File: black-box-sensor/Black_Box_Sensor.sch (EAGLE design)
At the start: 58 parts, among them J1 104031-0811, J2 UX60-MB-5S8, J3 B4B-PH-SM4-TBT(LF)(SN), U1 ADXL375, U2 ADXL375, U3 ATMEGA32U4-AU, U4 FXAS21002CQR1, U6 NL27WZ32USG, U7 LT1129CST-5#PBF, U8 AD8426ACPZ-WP, U9 TXU0304

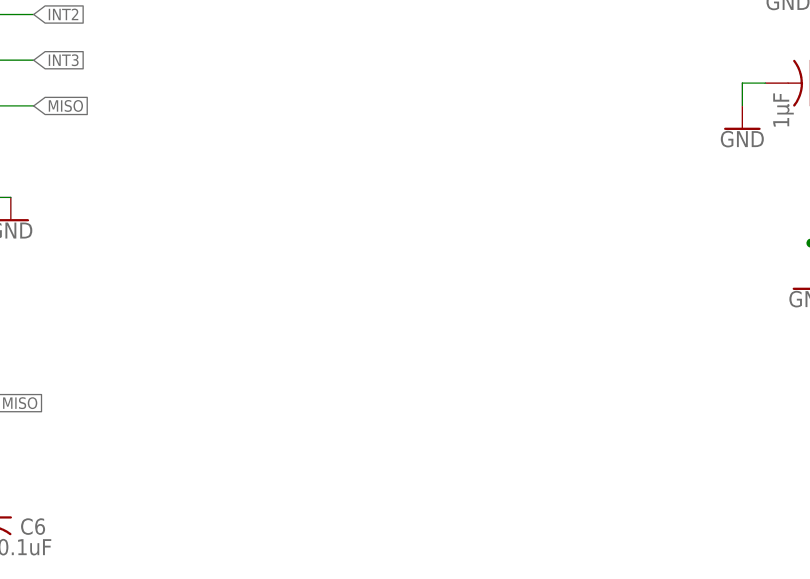
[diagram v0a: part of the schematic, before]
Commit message: Gyroscope added to schematic
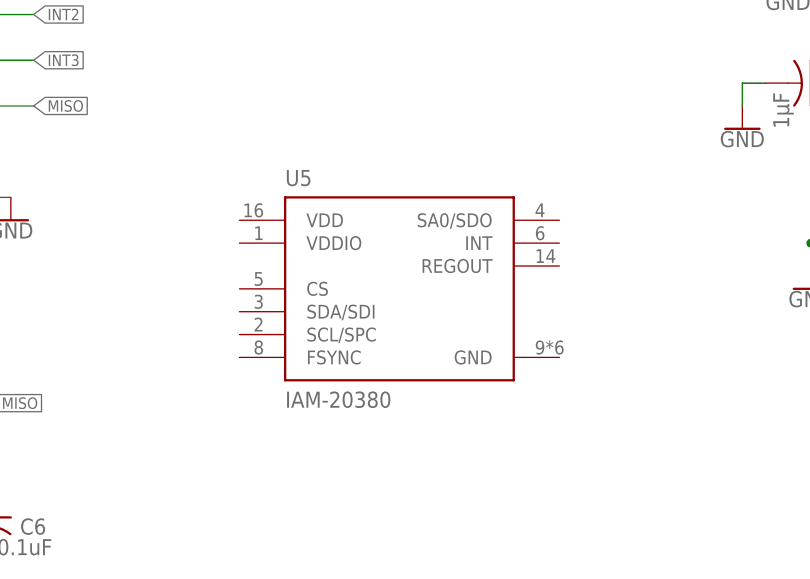
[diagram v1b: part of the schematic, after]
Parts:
- added U5: IAM-20380, BBS_Library:IAM-20380
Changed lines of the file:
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@@
 <part name="P+9" library="supply1" library_urn="urn:adsk.eagle:library:371" deviceset="+5V" device=""/>
 <part name="R16" library="rcl" library_urn="urn:adsk.eagle:library:334" deviceset="R-US_" device="R0603" package3d_urn="urn:adsk.eagle:package:23555/3" value="10k"/>
+<part name="U5" library="BBS_Library" deviceset="IAM-20380" device=""/>
 </parts>
 <sheets>
@@
 <attribute name="VALUE" x="170.942" y="92.71" size="1.778" layer="96" rot="R90"/>
 </instance>
+<instance part="U5" gate="G$1" x="114.3" y="25.4" smashed="yes">
+<attribute name="NAME" x="101.6" y="36.83" size="1.778" layer="95"/>
+<attribute name="VALUE" x="101.6" y="13.97" size="1.78078125" layer="96" align="top-left"/>
+</instance>
 </instances>

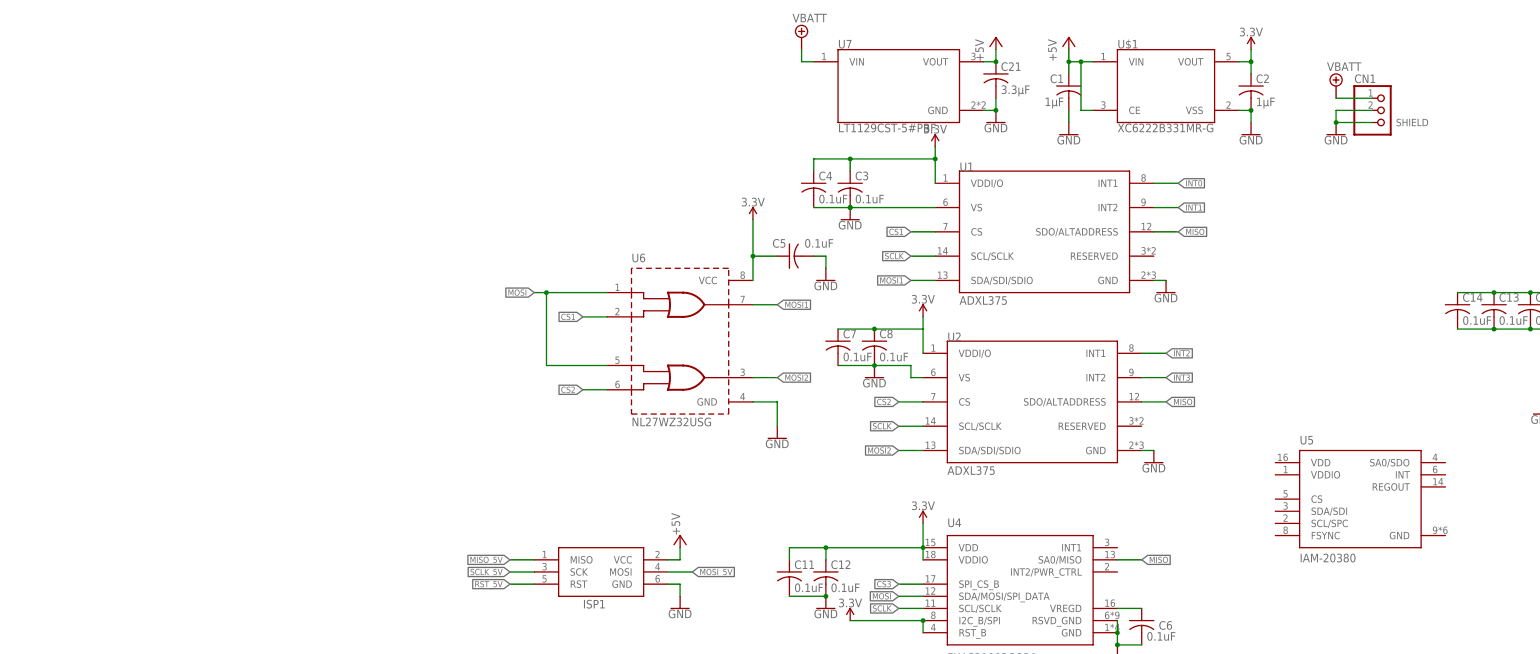
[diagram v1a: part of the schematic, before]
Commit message: Added gyroscope
missing some connections, and its capacitors may not have the right footprint, will follow up with Valentin later about it
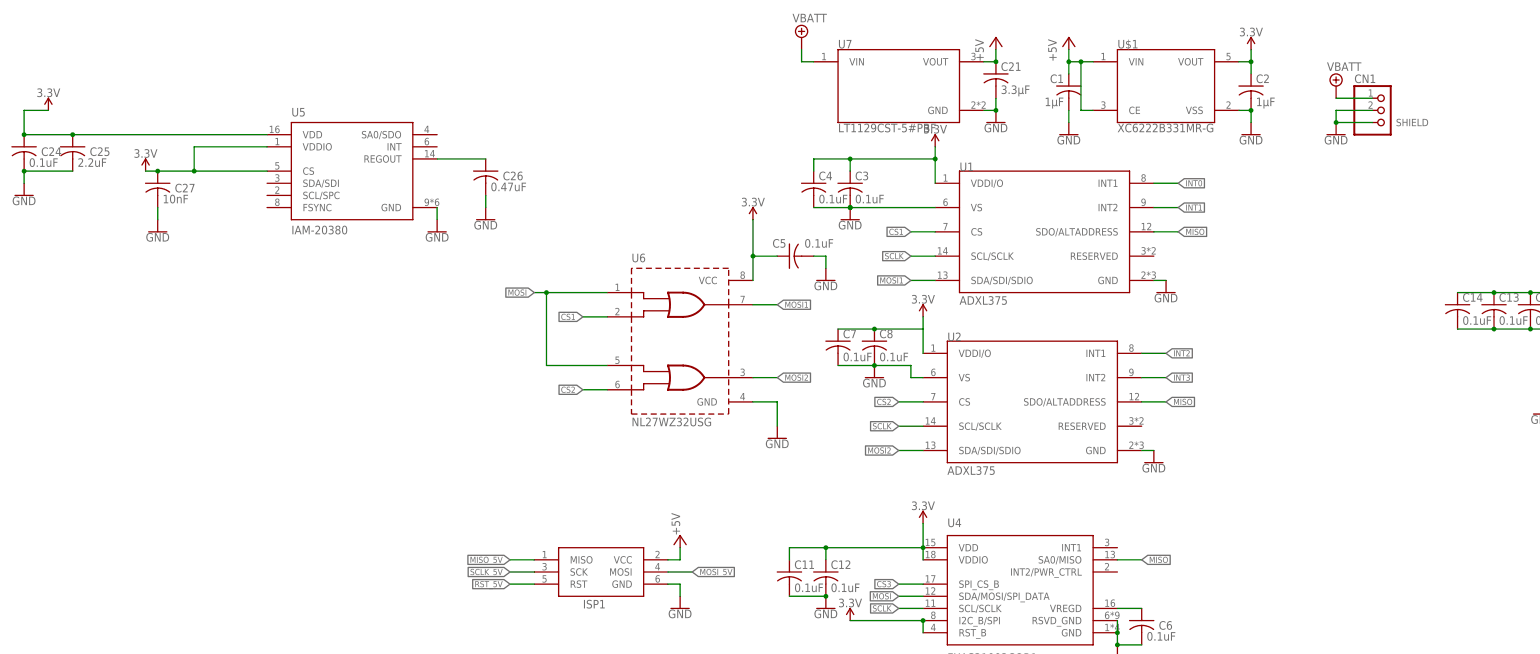
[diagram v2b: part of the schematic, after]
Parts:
- added C24: 0.1uF, rcl:C-USC0603
- added C25: 2.2uF, rcl:C-USC0603
- added C26: 0.47uF, rcl:C-USC0603
- added C27: 10nF, rcl:C-USC0603
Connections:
- new net N$10: C26.1, U5.REGOUT
- net 3.3V: now also C24.1, C25.1, C27.1, U5.CS, U5.VDD, U5.VDDIO
- net GND: now also C24.2, C25.2, C26.2, C27.2, U5.GND
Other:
- moved on the sheet: U5

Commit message: Gyroscope wiring complete
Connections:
- new net FSYNC_GYRO: U3.PB4(ADC11)
- new net INT6: U3.PE6(INT.6/AIN0)
- new net N$11: U5.INT
- new net N$12: U5.FSYNC
- net GND: now also U5.SA0/SDO
- net INT0: now also U5.SCL/SPC
- net INT1: now also U5.SDA/SDI

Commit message: clean schematic for DR
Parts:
- removed C11, C12: 0.1uF, rcl:C-USC0603K
- removed C6: 0.1uF, rcl:C-USC0603
- removed U4: FXAS21002CQR1, BBS_Library:FXAS21002CQR1
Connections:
- removed net FSYNC_GYRO: U3.PB4(ADC11)
- removed net N$1: C6.1, U4.VREGD
- removed net N$11: U5.INT
- removed net N$12: U5.FSYNC
- new net FSYNC: U3.PB4(ADC11), U5.FSYNC
- net 3.3V: no longer C11.1, C12.1, U4.I2C_B/SPI, U4.RST_B, U4.VDD, U4.VDDIO
- net CS3: no longer U4.SPI_CS_B
- net GND: no longer C11.2, C12.2, C6.2, U4.GND, U4.RSVD_GND
- net INT6: now also U5.INT
- net MISO: no longer U4.SA0/MISO
- net MOSI: no longer U4.SDA/MOSI/SPI_DATA
- net SCLK: no longer U4.SCL/SCLK
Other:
- moved on the sheet: C1, C18, C19, C2, C21, C24, C25, C26, C27, CN1, J3, JP1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

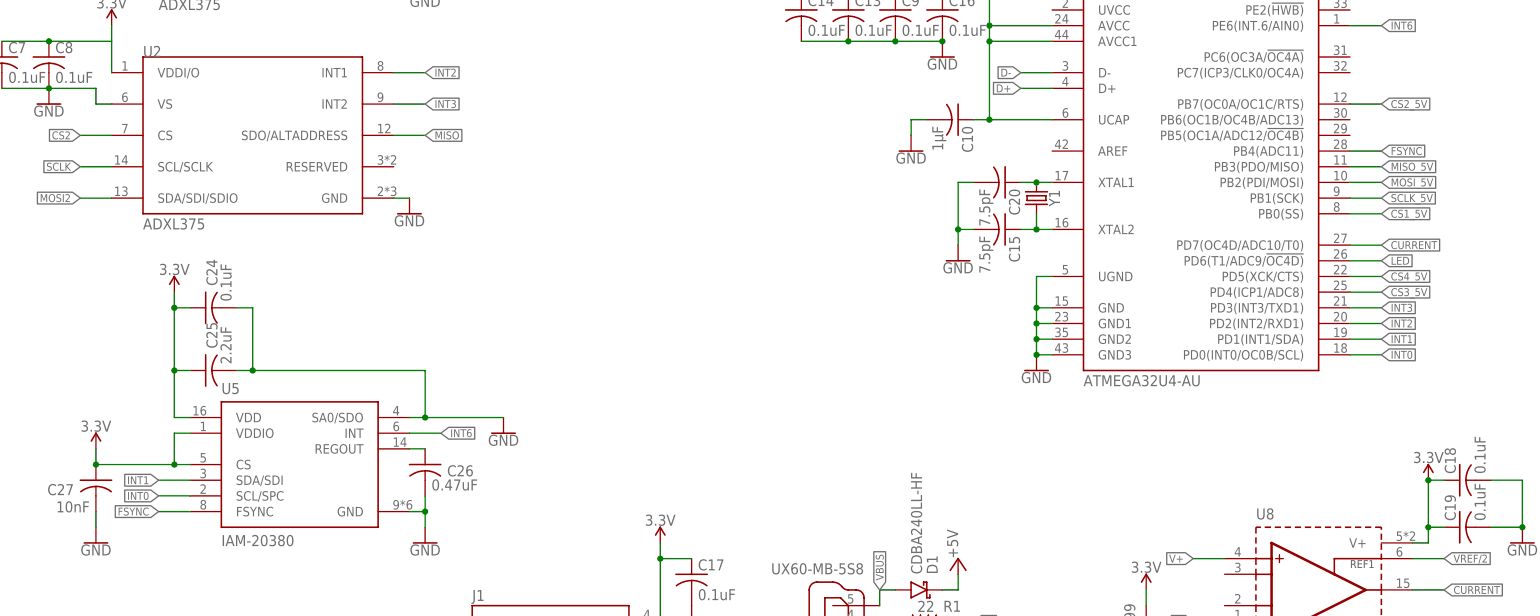
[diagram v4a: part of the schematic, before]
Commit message: fix some pin connections, but possibly will switch microcontroller
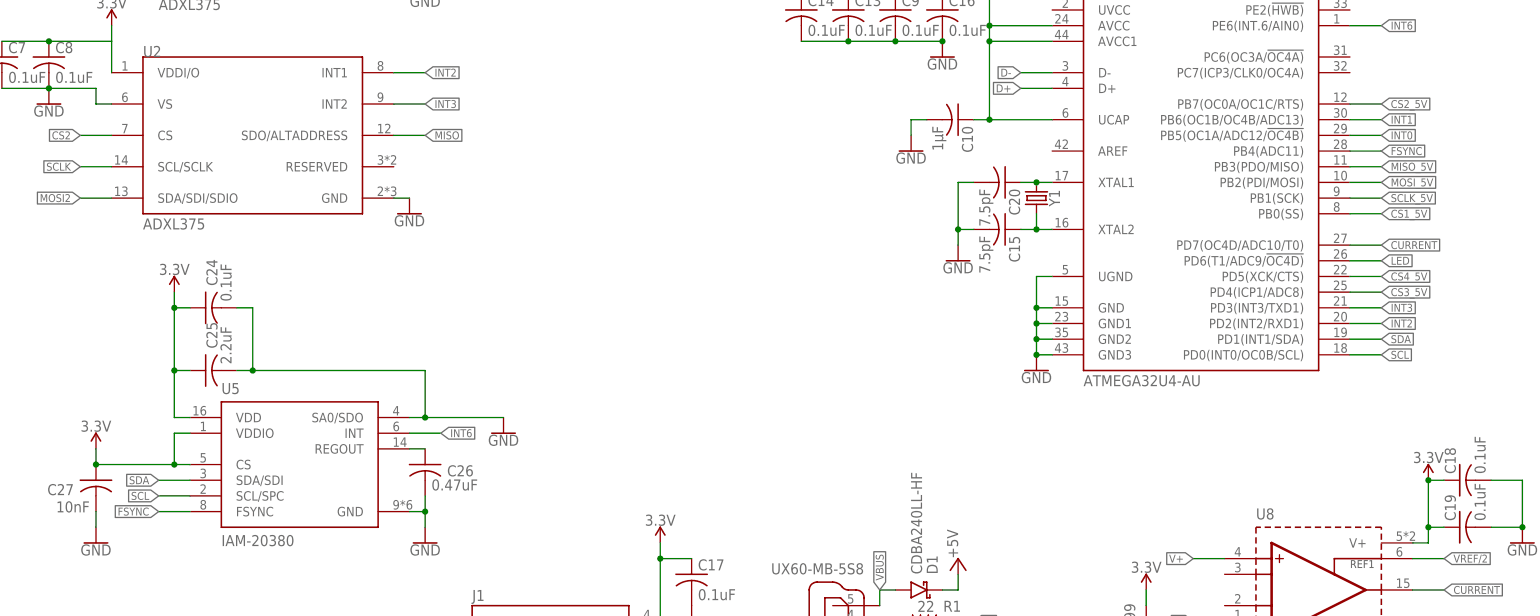
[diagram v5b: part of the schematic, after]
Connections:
- new net SCL: U3.PD0(INT0/OC0B/SCL), U5.SCL/SPC
- new net SDA: U3.PD1(INT1/SDA), U5.SDA/SDI
- net INT0: now also U3.PB5(OC1A/ADC12/!OC4B); no longer U3.PD0(INT0/OC0B/SCL), U5.SCL/SPC
- net INT1: now also U3.PB6(OC1B/OC4B/ADC13); no longer U3.PD1(INT1/SDA), U5.SDA/SDI
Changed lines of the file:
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@@
 </segment>
 </net>
-<net name="INT1" class="0">
+<net name="SDA" class="0">
 <segment>
 <pinref part="U3" gate="G$1" pin="PD1(INT1/SDA)"/>
@@
 </segment>
 <segment>
-<pinref part="U1" gate="ADXL375BCCZ-RL7" pin="INT2"/>
-<wire x1="71.12" y1="86.36" x2="76.2" y2="86.36" width="0.1524" layer="91"/>
-<label x="76.2" y="86.36" size="1.27" layer="95" xref="yes"/>
-</segment>
-<segment>
 <wire x1="35.56" y1="-10.16" x2="30.48" y2="-10.16" width="0.1524" layer="91"/>
 <label x="30.48" y="-10.16" size="1.27" layer="95" rot="R180" xref="yes"/>
@@
 </segment>
 </net>
-<net name="INT0" class="0">
+<net name="SCL" class="0">
 <segment>
 <pinref part="U3" gate="G$1" pin="PD0(INT0/OC0B/SCL)"/>
 <wire x1="223.52" y1="10.16" x2="228.6" y2="10.16" width="0.1524" layer="91"/>
 <label x="228.6" y="10.16" size="1.27" layer="95" xref="yes"/>
-</segment>
-<segment>
-<pinref part="U1" gate="ADXL375BCCZ-RL7" pin="INT1"/>
-<wire x1="71.12" y1="91.44" x2="76.2" y2="91.44" width="0.1524" layer="91"/>
-<label x="76.2" y="91.44" size="1.27" layer="95" xref="yes"/>
 </segment>
 <segment>
@@
 </segment>
 </net>
+<net name="INT0" class="0">
+<segment>
+<pinref part="U1" gate="ADXL375BCCZ-RL7" pin="INT1"/>
+<wire x1="71.12" y1="91.44" x2="76.2" y2="91.44" width="0.1524" layer="91"/>
+<label x="76.2" y="91.44" size="1.27" layer="95" xref="yes"/>
+</segment>
+<segment>
+<pinref part="U3" gate="G$1" pin="PB5(OC1A/ADC12/!OC4B)"/>
+<wire x1="223.52" y1="45.72" x2="228.6" y2="45.72" width="0.1524" layer="91"/>
+<label x="228.6" y="45.72" size="1.27" layer="95" xref="yes"/>
+</segment>
+</net>
+<net name="INT1" class="0">
+<segment>
+<pinref part="U1" gate="ADXL375BCCZ-RL7" pin="INT2"/>
+<wire x1="71.12" y1="86.36" x2="76.2" y2="86.36" width="0.1524" layer="91"/>
+<label x="76.2" y="86.36" size="1.27" layer="95" xref="yes"/>
+</segment>
+<segment>
+<pinref part="U3" gate="G$1" pin="PB6(OC1B/OC4B/ADC13)"/>
+<wire x1="223.52" y1="48.26" x2="228.6" y2="48.26" width="0.1524" layer="91"/>
+<label x="228.6" y="48.26" size="1.27" layer="95" xref="yes"/>
+</segment>
+</net>

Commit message: add to bbs lib and schematic
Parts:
- added U4: ATSAMD21G17A-AUMICROCHIP_TECHNOLOGY_-_ATMEL_ATSAMD21G17A-AU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, BBS_Library:ATSAMD21G17A-AUMICROCHIP_TECHNOLOGY_-_ATMEL_ATSAMD21G17A-AU_0_0
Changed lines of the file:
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@@
 <part name="GND36" library="SparkFun-PowerSymbols" deviceset="GND" device=""/>
 <part name="GND37" library="SparkFun-PowerSymbols" deviceset="GND" device=""/>
+<part name="U4" library="BBS_Library" deviceset="ATSAMD21G17A-AU" device="MICROCHIP_TECHNOLOGY_-_ATMEL_ATSAMD21G17A-AU_0_0"/>
 </parts>
 <sheets>
@@
 <attribute name="VALUE" x="86.36" y="-2.794" size="1.778" layer="96" align="top-center"/>
 </instance>
+<instance part="U4" gate="G$0" x="269.24" y="200.66" smashed="yes">
+<attribute name="NAME" x="271.78" y="198.12" size="2.54" layer="95" align="top-left"/>
+</instance>
 </instances>
